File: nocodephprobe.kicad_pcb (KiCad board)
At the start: 2 copper layers, 76 x 80.9 mm, 30 parts, among them J1 RF1-01 BNC, J2 10K, Q1 2N7002, U1 LMV358a, U2 ICL7106CPL, U3 MCP1501T-10E/CHY, U4 VI-302-DP-RC-S

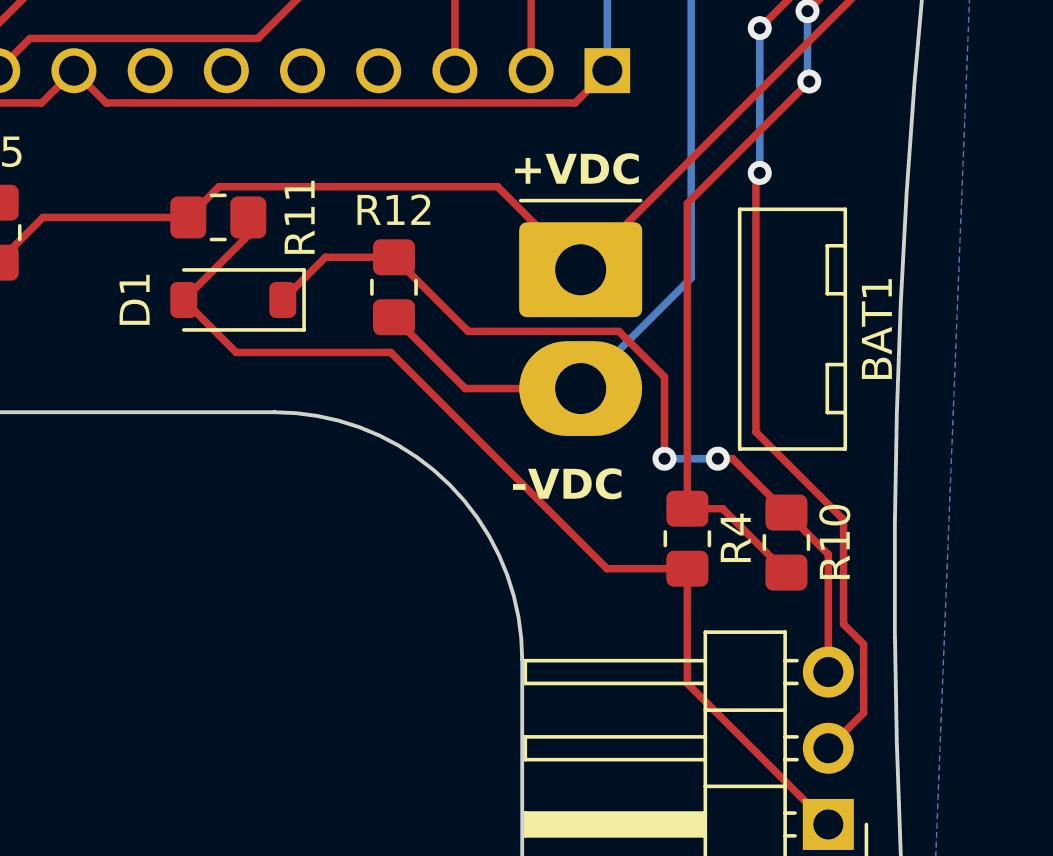
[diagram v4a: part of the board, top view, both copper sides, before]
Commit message: pcb: eliminate 2 vias
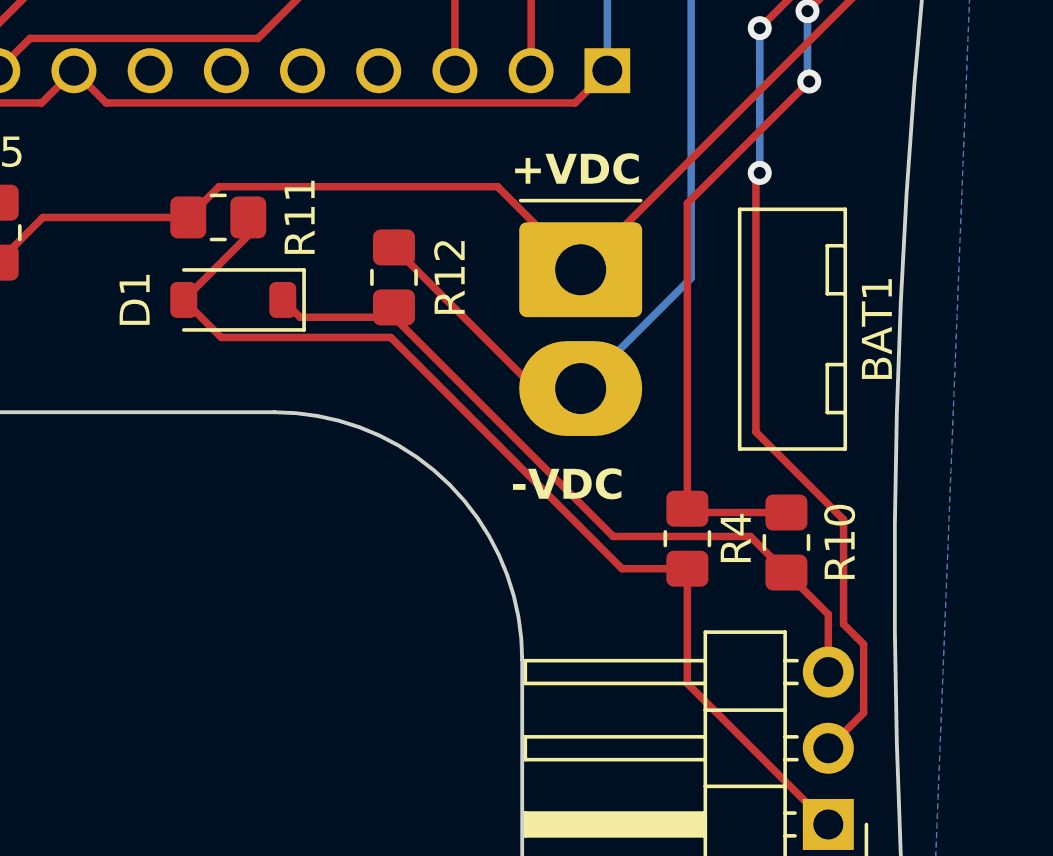
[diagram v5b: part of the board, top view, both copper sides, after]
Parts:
- moved R12 0.33 mm to (165.6, 107.8), turned to -90 degrees
- turned R10 to 90 degrees
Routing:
- net Net-(D1-K): track 28.4 -> 24.9 mm, vias 2 -> 0
- net -VDC: track 88.2 -> 89.2 mm
- net Net-(U1B-+): track 68.3 -> 67.4 mm
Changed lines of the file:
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@@
   )
   (footprint "Resistor_SMD:R_0805_2012Metric_Pad1.20x1.40mm_HandSolder" (layer "F.Cu")
-    (at 165.608 108.077 90)
+    (at 165.608 107.75 -90)
     (descr "Resistor SMD 0805 (2012 Metric), square (rectangular) end terminal, IPC_7351 nominal with elongated pad for handsoldering. (Body size source: IPC-SM-782 page 72, https://www.pcb-3d.com/wordpress/wp-content/uploads/ipc-sm-782a_amendment_1_and_2.pdf), generated with kicad-footprint-generator")
     (tags "resistor handsolder")
@@
     (property "ki_keywords" "R res resistor")
     (attr smd)
-    (fp_text reference "R12" (at 2.54 0 180) (layer "F.SilkS")
+    (fp_text reference "R12" (at 0 -1.892 90) (layer "F.SilkS")
         (effects (font (size 1 1) (thickness 0.15)))
     )
@@
     (fp_line (start 1 0.625) (end -1 0.625)
       (stroke (width 0.1) (type solid)) (layer "F.Fab"))
-    (pad "1" smd roundrect (at -1 0 90) (size 1.2 1.4) (layers "F.Cu" "F.Paste" "F.Mask") (roundrect_rratio 0.2083333333)
+    (pad "1" smd roundrect (at -1 0 270) (size 1.2 1.4) (layers "F.Cu" "F.Paste" "F.Mask") (roundrect_rratio 0.2083333333)
       (net 2 "-VDC") (pintype "passive"))
-    (pad "2" smd roundrect (at 1 0 90) (size 1.2 1.4) (layers "F.Cu" "F.Paste" "F.Mask") (roundrect_rratio 0.2083333333)
+    (pad "2" smd roundrect (at 1 0 270) (size 1.2 1.4) (layers "F.Cu" "F.Paste" "F.Mask") (roundrect_rratio 0.2083333333)
       (net 12 "Net-(D1-K)") (pintype "passive"))
     (model "${KICAD6_3DMODEL_DIR}/Resistor_SMD.3dshapes/R_0805_2012Metric.wrl"
@@
   )
   (footprint "Resistor_SMD:R_0805_2012Metric_Pad1.20x1.40mm_HandSolder" (layer "F.Cu")
-    (at 178.689 116.586 -90)
+    (at 178.689 116.586 90)
     (descr "Resistor SMD 0805 (2012 Metric), square (rectangular) end terminal, IPC_7351 nominal with elongated pad for handsoldering. (Body size source: IPC-SM-782 page 72, https://www.pcb-3d.com/wordpress/wp-content/uploads/ipc-sm-782a_amendment_1_and_2.pdf), generated with kicad-footprint-generator")
     (tags "resistor handsolder")
@@
     (property "ki_keywords" "R res resistor")
     (attr smd)
-    (fp_text reference "R10" (at 0 -1.65 90) (layer "F.SilkS")
+    (fp_text reference "R10" (at 0 1.811 90) (layer "F.SilkS")
         (effects (font (size 1 1) (thickness 0.15)))
     )
@@
     (fp_line (start 1 0.625) (end -1 0.625)
       (stroke (width 0.1) (type solid)) (layer "F.Fab"))
-    (pad "1" smd roundrect (at -1 0 270) (size 1.2 1.4) (layers "F.Cu" "F.Paste" "F.Mask") (roundrect_rratio 0.2083333333)
+    (pad "1" smd roundrect (at -1 0 90) (size 1.2 1.4) (layers "F.Cu" "F.Paste" "F.Mask") (roundrect_rratio 0.2083333333)
       (net 12 "Net-(D1-K)") (pintype "passive"))
-    (pad "2" smd roundrect (at 1 0 270) (size 1.2 1.4) (layers "F.Cu" "F.Paste" "F.Mask") (roundrect_rratio 0.2083333333)
+    (pad "2" smd roundrect (at 1 0 90) (size 1.2 1.4) (layers "F.Cu" "F.Paste" "F.Mask") (roundrect_rratio 0.2083333333)
       (net 19 "Net-(U1B-+)") (pintype "passive"))
     (model "${KICAD6_3DMODEL_DIR}/Resistor_SMD.3dshapes/R_0805_2012Metric.wrl"
@@
   (segment (start 122.1955 93.218) (end 124.46 93.218) (width 0.254) (layer "F.Cu") (net 1))
   (segment (start 169.062 104.725) (end 159.775 104.725) (width 0.25) (layer "F.Cu") (net 1))
+  (segment (start 170.312 111.454) (end 171.831 111.454) (width 0.25) (layer "F.Cu") (net 2))
   (segment (start 160.063 75.692) (end 160.063 77.935) (width 0.25) (layer "F.Cu") (net 2))
-  (segment (start 167.985 111.454) (end 171.831 111.454) (width 0.25) (layer "F.Cu") (net 2))
   (segment (start 160.063 77.935) (end 160.02 77.978) (width 0.25) (layer "F.Cu") (net 2))
   (segment (start 160.6305 66.9665) (end 167.767 66.9665) (width 0.25) (layer "F.Cu") (net 2))
+  (segment (start 165.608 106.75) (end 170.312 111.454) (width 0.25) (layer "F.Cu") (net 2))
   (segment (start 159.196 65.532) (end 160.6305 66.9665) (width 0.25) (layer "F.Cu") (net 2))
-  (segment (start 165.608 109.077) (end 167.985 111.454) (width 0.25) (layer "F.Cu") (net 2))
   (via (at 167.767 66.9665) (size 0.8) (drill 0.4) (layers "F.Cu" "B.Cu") (net 2))
   (segment (start 171.995 81.383991) (end 171.995 83.222) (width 0.25) (layer "B.Cu") (net 2))
@@
   (segment (start 166.497 77.724) (end 166.497 84.583396) (width 0.25) (layer "F.Cu") (net 11))
   (segment (start 159.647695 79.103) (end 163.025991 79.103) (width 0.25) (layer "F.Cu") (net 11))
-  (segment (start 163.323 107.077) (end 165.608 107.077) (width 0.25) (layer "F.Cu") (net 12))
-  (segment (start 176.895 113.792) (end 178.689 115.586) (width 0.25) (layer "F.Cu") (net 12))
-  (segment (start 176.403 113.792) (end 176.895 113.792) (width 0.25) (layer "F.Cu") (net 12))
-  (segment (start 174.625 111.067) (end 174.625 113.792) (width 0.25) (layer "F.Cu") (net 12))
-  (segment (start 173.107 109.549) (end 174.625 111.067) (width 0.25) (layer "F.Cu") (net 12))
-  (segment (start 178.689 115.586) (end 180.086 116.983) (width 0.25) (layer "F.Cu") (net 12))
-  (segment (start 165.608 107.077) (end 168.08 109.549) (width 0.25) (layer "F.Cu") (net 12))
-  (segment (start 168.08 109.549) (end 173.107 109.549) (width 0.25) (layer "F.Cu") (net 12))
-  (segment (start 180.086 116.983) (end 180.086 120.904) (width 0.25) (layer "F.Cu") (net 12))
-  (segment (start 161.9 108.5) (end 163.323 107.077) (width 0.25) (layer "F.Cu") (net 12))
-  (via (at 176.403 113.792) (size 0.8) (drill 0.4) (layers "F.Cu" "B.Cu") (net 12))
-  (via (at 174.625 113.792) (size 0.8) (drill 0.4) (layers "F.Cu" "B.Cu") (net 12))
-  (segment (start 174.625 113.792) (end 176.403 113.792) (width 0.25) (layer "B.Cu") (net 12))
+  (segment (start 178.689 117.586) (end 177.487 116.384) (width 0.25) (layer "F.Cu") (net 12))
+  (segment (start 162.477 109.077) (end 161.9 108.5) (width 0.25) (layer "F.Cu") (net 12))
+  (segment (start 180.086 120.904) (end 180.086 118.983) (width 0.25) (layer "F.Cu") (net 12))
+  (segment (start 177.487 116.384) (end 172.915 116.384) (width 0.25) (layer "F.Cu") (net 12))
+  (segment (start 172.915 116.384) (end 165.608 109.077) (width 0.25) (layer "F.Cu") (net 12))
+  (segment (start 165.608 108.75) (end 165.281 109.077) (width 0.25) (layer "F.Cu") (net 12))
+  (segment (start 180.086 118.983) (end 178.689 117.586) (width 0.25) (layer "F.Cu") (net 12))
+  (segment (start 165.608 109.077) (end 165.608 108.75) (width 0.25) (layer "F.Cu") (net 12))
+  (segment (start 165.281 109.077) (end 162.477 109.077) (width 0.25) (layer "F.Cu") (net 12))
   (segment (start 143.315 101.435) (end 142.367 102.383) (width 0.25) (layer "F.Cu") (net 13))
   (segment (start 154.94 100.858) (end 153.865 101.933) (width 0.25) (layer "F.Cu") (net 13))
@@
   (segment (start 125.449695 108.975) (end 128.172 108.975) (width 0.25) (layer "F.Cu") (net 18))
   (segment (start 164.146 65.532) (end 173.150432 65.532) (width 0.25) (layer "F.Cu") (net 19))
+  (segment (start 175.514 115.586) (end 175.387 115.459) (width 0.25) (layer "F.Cu") (net 19))
   (segment (start 173.150432 65.532) (end 180.41 72.791568) (width 0.25) (layer "F.Cu") (net 19))
+  (segment (start 178.689 115.586) (end 175.514 115.586) (width 0.25) (layer "F.Cu") (net 19))
   (segment (start 180.41 97.479) (end 180.41 97.8556) (width 0.25) (layer "F.Cu") (net 19))
-  (segment (start 176.562 115.459) (end 178.689 117.586) (width 0.25) (layer "F.Cu") (net 19))
   (segment (start 180.41 72.791568) (end 180.41 97.479) (width 0.25) (layer "F.Cu") (net 19))
-  (segment (start 175.387 115.459) (end 176.562 115.459) (width 0.25) (layer "F.Cu") (net 19))
   (segment (start 175.387 105.283) (end 175.387 115.459) (width 0.25) (layer "F.Cu") (net 19))
   (segment (start 179.451 101.219) (end 175.387 105.283) (width 0.25) (layer "F.Cu") (net 19))
@@
   (segment (start 123.19 68.834) (end 123.19 63.5) (width 0.25) (layer "F.Cu") (net 57))
   (segment (start 160.75 106.35) (end 160.75 105.75) (width 0.25) (layer "F.Cu") (net 58))
-  (segment (start 172.709 117.459) (end 165.5 110.25) (width 0.25) (layer "F.Cu") (net 58))
   (segment (start 180.086 125.984) (end 175.387 121.285) (width 0.25) (layer "F.Cu") (net 58))
-  (segment (start 175.387 117.459) (end 172.709 117.459) (width 0.25) (layer "F.Cu") (net 58))
-  (segment (start 160.35 110.25) (end 158.6 108.5) (width 0.25) (layer "F.Cu") (net 58))
-  (segment (start 165.5 110.25) (end 160.35 110.25) (width 0.25) (layer "F.Cu") (net 58))
+  (segment (start 173.209 117.459) (end 165.5 109.75) (width 0.25) (layer "F.Cu") (net 58))
+  (segment (start 165.5 109.75) (end 159.85 109.75) (width 0.25) (layer "F.Cu") (net 58))
+  (segment (start 175.387 117.459) (end 173.209 117.459) (width 0.25) (layer "F.Cu") (net 58))
+  (segment (start 159.85 109.75) (end 158.6 108.5) (width 0.25) (layer "F.Cu") (net 58))
   (segment (start 158.6 108.5) (end 160.75 106.35) (width 0.25) (layer "F.Cu") (net 58))
   (segment (start 175.387 121.285) (end 175.387 117.459) (width 0.25) (layer "F.Cu") (net 58))

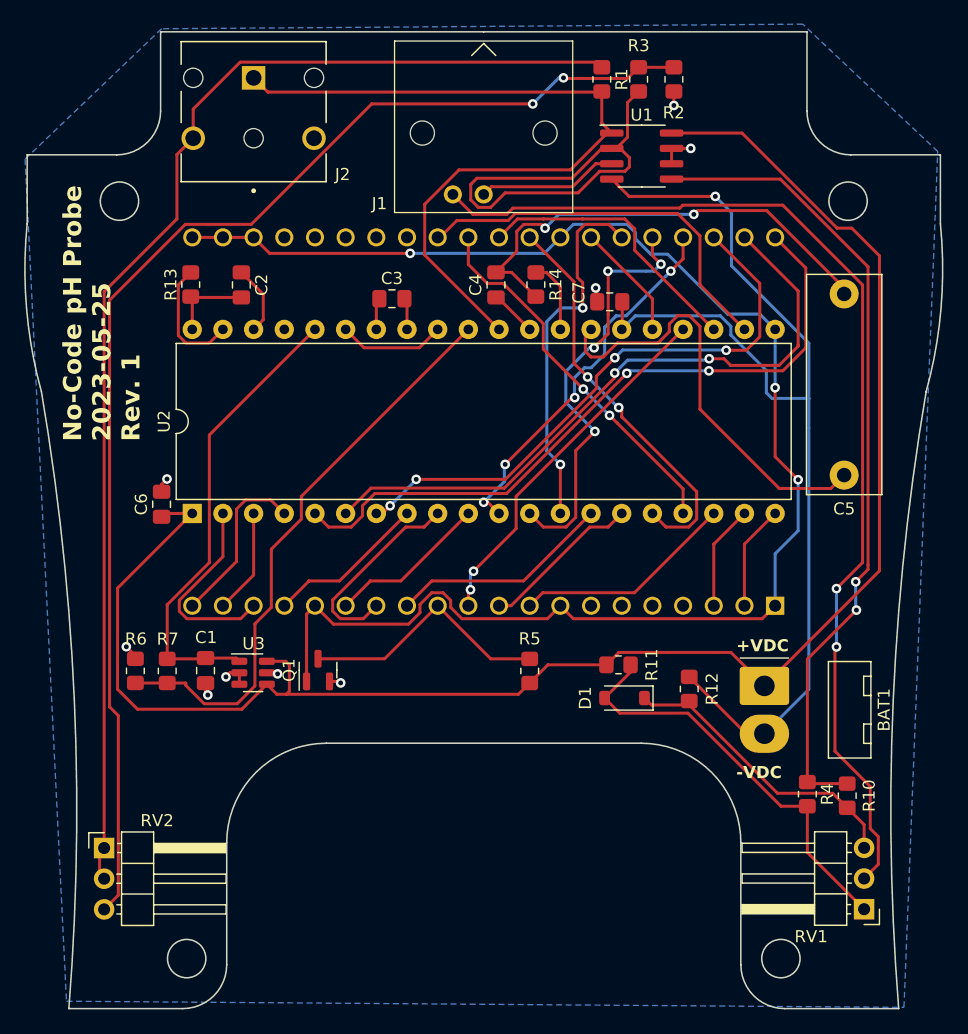
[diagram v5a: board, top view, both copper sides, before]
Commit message: Fix op-amp power supply
Add an 7805 linear regulator to keep voltage within max supply, and add
decoupling caps.
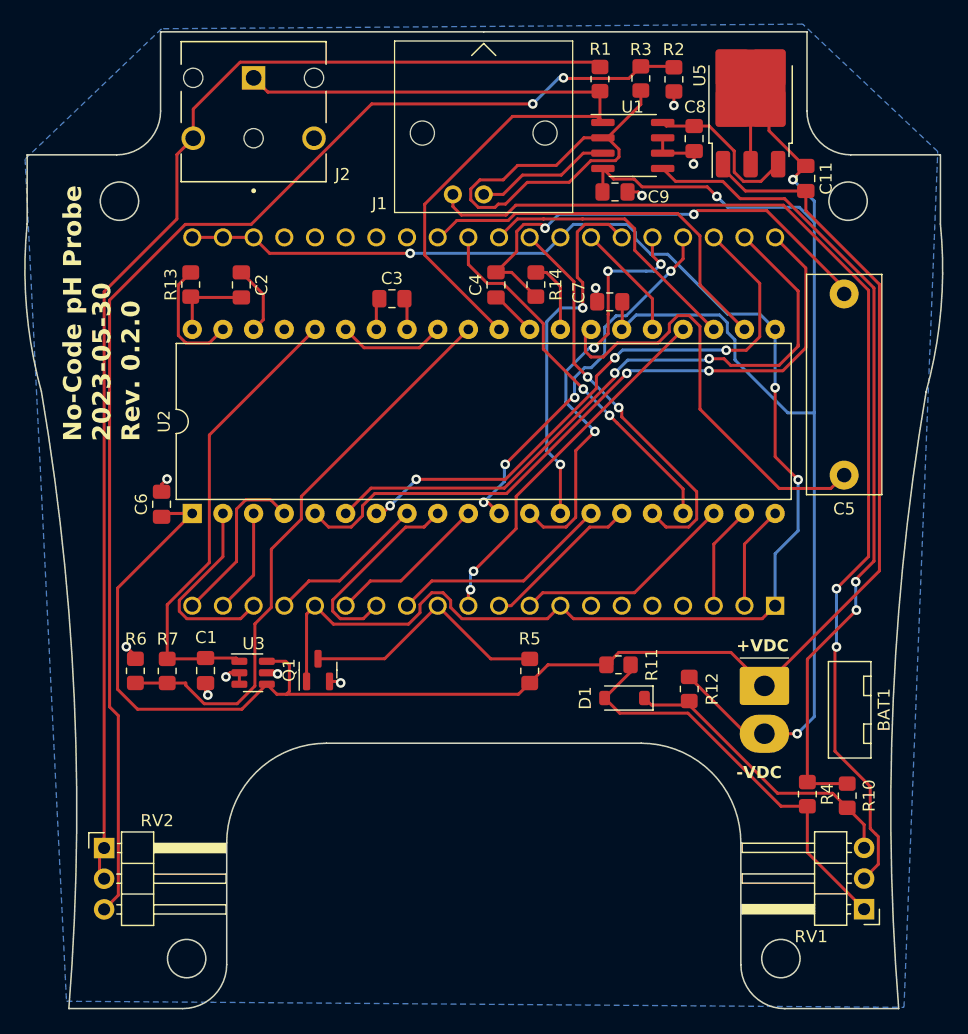
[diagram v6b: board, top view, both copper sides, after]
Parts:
- added C11: 0.33uF, Capacitor_SMD:C_0805_2012Metric_Pad1.18x1.45mm_HandSolder, F.Cu at (175.3, 65.5)
- added C8: 0.1uF, Capacitor_SMD:C_0805_2012Metric_Pad1.18x1.45mm_HandSolder, F.Cu at (166.0, 62.2)
- added C9: 0.1uF, Capacitor_SMD:C_0805_2012Metric_Pad1.18x1.45mm_HandSolder, F.Cu at (159.5, 66.6)
- added U5: L7805, Package_TO_SOT_SMD:TO-252-3_TabPin2, F.Cu at (170.7, 59.3)
- moved U1 1.15 mm to (160.9, 62.8)
- moved R3 0.20 mm to (161.6, 57.2), turned to 90 degrees
- moved R1 0.15 mm to (158.2, 57.3)
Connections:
- R3 pad 1: Net-(R2-Pad2) -> Net-(U1A--)
- R3 pad 2: Net-(U1A--) -> Net-(R2-Pad2)
- U1 pad 8: +VDC -> +5V
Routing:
- net -VDC: track 89.2 -> 116.9 mm, vias 1 -> 3
- net +5V: track 0.00 -> 13.2 mm
- net +VDC: track 143.1 -> 137.6 mm
- net GND: track 21.8 -> 25.3 mm, vias 9 -> 10
- net Net-(U1A--): track 37.4 -> 35.3 mm
- net /scaled: track 64.0 -> 62.8 mm
- net Net-(J1-Ext): track 89.7 -> 90.8 mm
- net Net-(U1B-+): track 67.4 -> 68.2 mm
